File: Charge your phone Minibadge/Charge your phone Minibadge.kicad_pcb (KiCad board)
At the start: 2 copper layers, 20.3 x 20.3 mm, 16 parts, among them J1 USB-C DFP, U1 MT3608, U2 TPS255x

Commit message: Finalize rev1
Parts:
- added G***: LOGO, LOGO, F.Cu at (111.1, 87.4)
- L1: footprint Inductor_SMD:L_Wuerth_MAPI-3020 -> Inductor_SMD:L_Taiyo-Yuden_MD-4040
- R1: value ? -> 750kΩ
- R2: value ? -> 100kΩ
- R4: value 59kΩ* -> 51kΩ
- U2: value TPS255x -> TPS2552
- moved U1 0.58 mm to (111.4, 85.0)
- moved R4 0.57 mm to (111.1, 90.4)
- moved L1 0.46 mm to (111.4, 80.8)
- moved C3 0.24 mm to (111.4, 77.3)
- moved D1 0.20 mm to (116.1, 79.6)
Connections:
- U2 pad 3: unconnected-(U2-EN-Pad3) -> GND
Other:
- board text added: "Low battery?"
- board text removed: "Charge your phone"

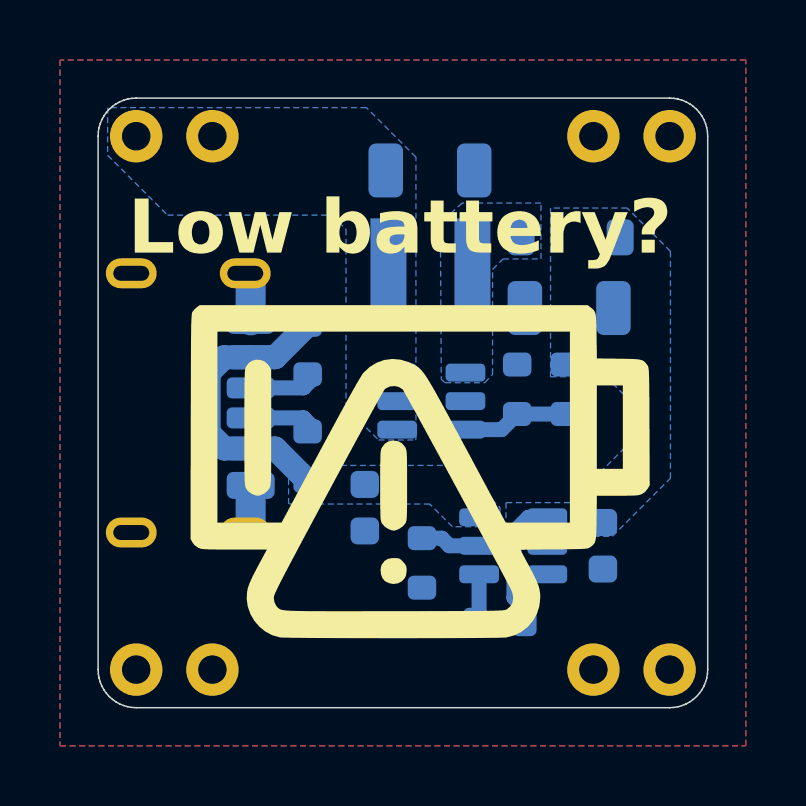
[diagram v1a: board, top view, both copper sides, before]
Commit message: Update silkscreen positions and text in PCB layout
Adjusted the positions of silkscreen reference designators for several components (R4, R5, R6, C1, C5, U1) and updated the vector font renderings for their labels in the KiCad PCB file. These changes improve silkscreen clarity and alignment on the board.
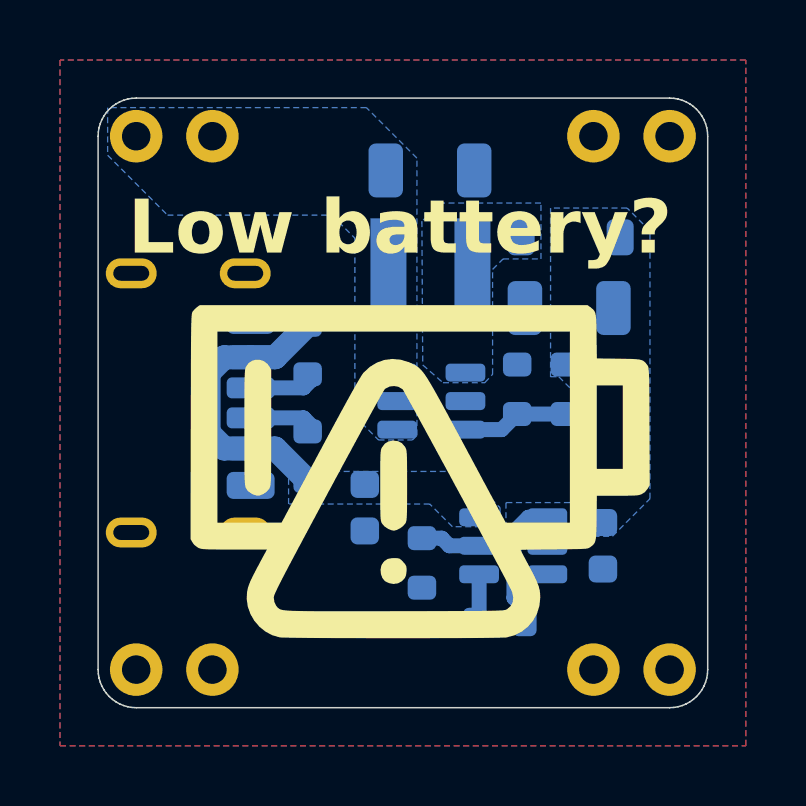
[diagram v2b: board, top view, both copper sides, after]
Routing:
- net GND: track 3.29 -> 0.00 mm
